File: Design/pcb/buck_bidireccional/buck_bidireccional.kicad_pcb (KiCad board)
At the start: 2 copper layers, 85 x 60 mm, 19 parts, among them J1 Conn_01x02_Pin, J2 Screw_Terminal_01x02, J3 Screw_Terminal_01x02, J4 Conn_01x02_Pin, Q1 NMOS, Q2 NMOS, U1 IR2184

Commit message: updated pcb
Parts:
- added C4: 4.7u, Capacitor_THT:CP_Radial_D5.0mm_P2.00mm, F.Cu at (154.5, 120.5)
- added J5: Screw_Terminal_01x02, TerminalBlock_Phoenix:TerminalBlock_Phoenix_MKDS-1,5-2-5.08_1x02_P5.08mm_Horizontal, F.Cu at (117.5, 126.1)
- added R6: 10k, Resistor_THT:R_Axial_DIN0207_L6.3mm_D2.5mm_P7.62mm_Horizontal, F.Cu at (128.2, 129.8)
- R4, R5: value 100k -> 10k
- moved Q2 35.6 mm to (139.7, 93.5), turned to 0 degrees
- moved R5 28.3 mm to (148.2, 98.4), turned to -90 degrees
- moved R3 18.3 mm to (122.2, 104.8)
- moved J1 18.0 mm to (133.2, 129.2), turned to 90 degrees
- moved D2 16.8 mm to (127.8, 104.8)
- moved R4 15.0 mm to (133.2, 96.9), turned to -90 degrees
- moved R1 14.1 mm to (149.5, 121.9), turned to -90 degrees
- moved R2 13.4 mm to (139.0, 105.6), turned to 90 degrees
- moved D3 12.8 mm to (143.5, 106.1), turned to 90 degrees
- moved Q1 12.3 mm to (127.7, 93.5)
- moved D4 11.7 mm to (137.7, 122.0)
- moved U1 10.6 mm to (133.2, 116.3), turned to 90 degrees
- moved C3 8.88 mm to (147.5, 112.8), turned to 0 degrees
- moved C1 7.58 mm to (125.8, 111.8)
- moved J3 6.37 mm to (115.9, 110.7)
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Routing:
- net GND: track 143.8 -> 0.00 mm
- net Net-(D2-K): track 12.8 -> 120.6 mm
- net Net-(D4-K): track 9.27 -> 109.4 mm
- net +12V: track 28.0 -> 88.6 mm
- net Net-(J4-Pin_2): track 132.8 -> 101.9 mm
- net Net-(D2-A): track 11.9 -> 27.4 mm
- net Net-(J1-Pin_2): track 33.8 -> 27.6 mm
- net Net-(J1-Pin_1): track 24.3 -> 18.6 mm
- net Net-(D3-K): track 10.8 -> 16.1 mm
- net Net-(J2-Pin_1): track 51.7 -> 56.4 mm
- net Net-(D3-A): track 11.1 -> 14.9 mm
- net Net-(J3-Pin_1): track 30.0 -> 29.2 mm
- added copper zone on F.Cu, net (none)
- added copper zone on F.Cu, net GND

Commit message: updates kiskas
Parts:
- moved J2 5.12 mm to (171.0, 127.2), turned to 0 degrees
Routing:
- net Net-(J2-Pin_1): track 56.4 -> 55.6 mm

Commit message: update kicad
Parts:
- C4: value 4.7u -> 100n
- moved J2 55.0 mm to (116.0, 127.2), turned to -90 degrees
- moved J5 51.1 mm to (168.5, 128.5)
- moved C2 48.4 mm to (125.2, 128.5), turned to -90 degrees
- moved J4 48.3 mm to (135.0, 131.8), turned to 90 degrees
- moved R3 48.2 mm to (168.3, 90.5), turned to 180 degrees
- moved J1 43.7 mm to (173.0, 111.0), turned to 180 degrees
- moved D2 41.9 mm to (168.3, 94.2), turned to 180 degrees
- moved R6 41.6 mm to (167.1, 114.8), turned to 180 degrees
- moved R2 38.5 mm to (176.8, 97.8)
- moved U1 36.5 mm to (167.1, 102.7), turned to -90 degrees
- moved R1 29.3 mm to (177.0, 111.9)
- moved R5 28.9 mm to (177.0, 101.7)
- moved D3 28.5 mm to (171.8, 102.1)
- moved L1 24.2 mm to (142.5, 108.8), turned to 90 degrees
- moved R4 20.8 mm to (154.0, 97.3), turned to 90 degrees
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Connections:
- C4 pad 1: Net-(D2-K) -> +12V
- C4 pad 2: Net-(J4-Pin_2) -> GND
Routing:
- net Net-(D2-K): track 120.6 -> 38.9 mm
- net Net-(D4-K): track 109.4 -> 32.9 mm
- net +12V: track 88.6 -> 27.8 mm
- net Net-(J2-Pin_1): track 55.6 -> 0.46 mm
- net Net-(D3-A): track 14.9 -> 65.1 mm
- net Net-(J3-Pin_1): track 29.2 -> 0.00 mm
- net Net-(D2-A): track 27.4 -> 40.5 mm
- net Net-(J4-Pin_2): track 101.9 -> 109.3 mm
- net Net-(D3-K): track 16.1 -> 21.1 mm
- net Net-(J1-Pin_2): track 27.6 -> 32.1 mm
- added copper zone on B.Cu, net +12V
- added copper zone on B.Cu, net GND
- added copper zone on B.Cu, net Net-(J2-Pin_1)
- added copper zone on B.Cu, net Net-(J3-Pin_1)
- added copper zone on B.Cu, net Net-(J4-Pin_2)
- removed copper zone on F.Cu, net (none)
- removed copper zone on F.Cu, net GND

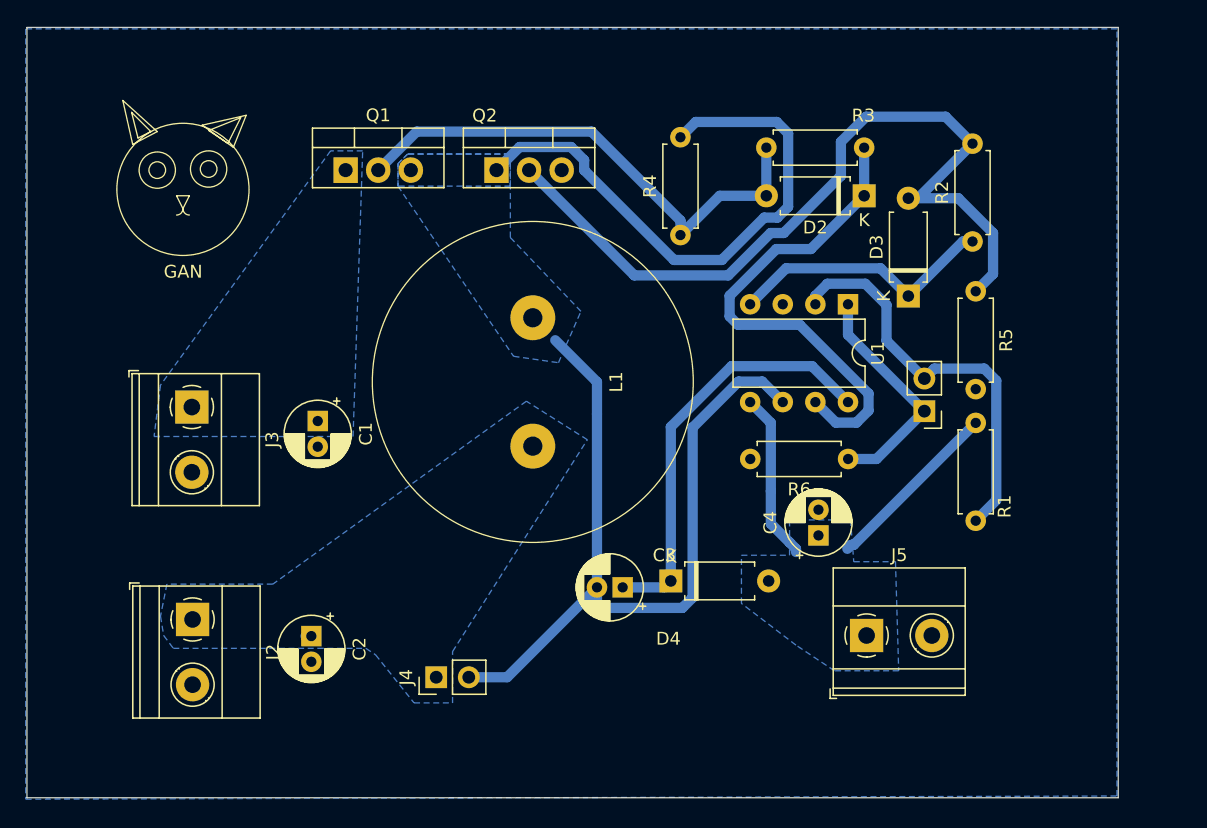
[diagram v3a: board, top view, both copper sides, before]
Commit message: updated kicad
MOSFET gate oscilloscope reading still missing
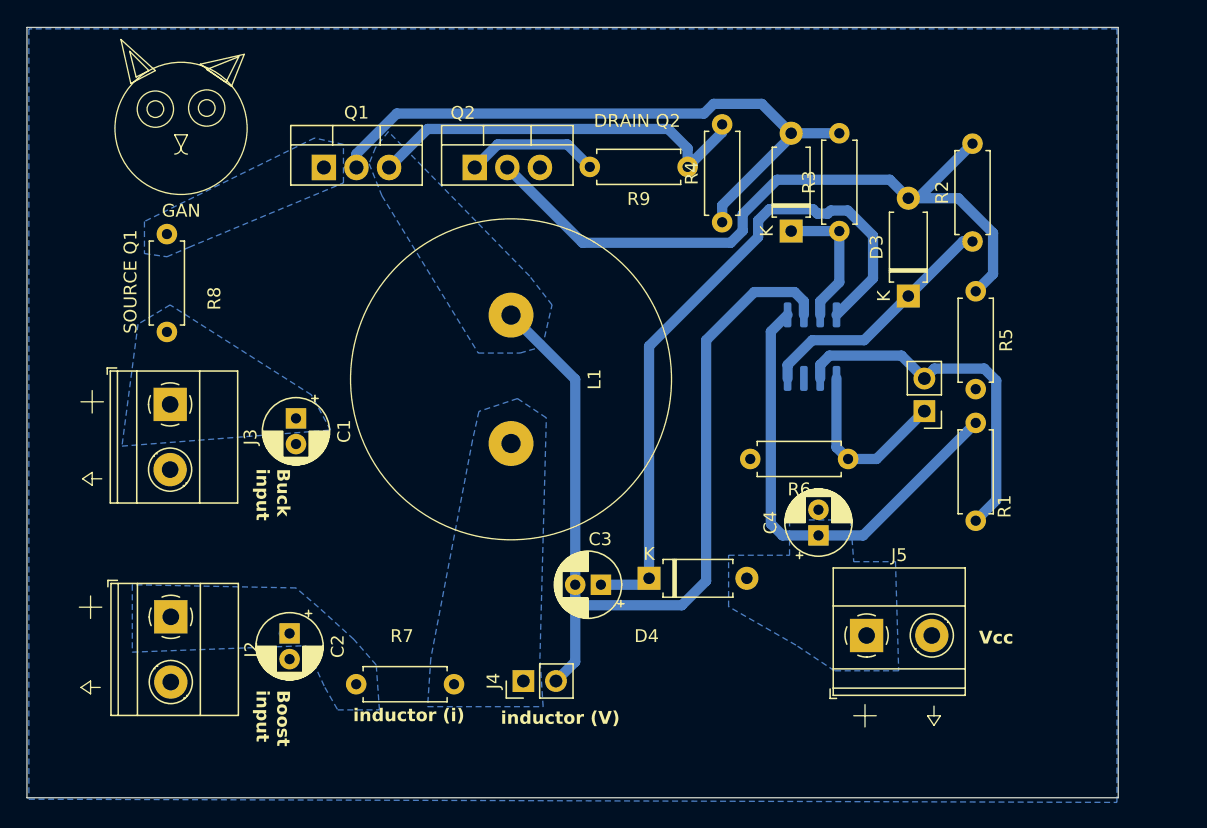
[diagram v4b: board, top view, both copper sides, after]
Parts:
- added R7: 1, Resistor_THT:R_Axial_DIN0207_L6.3mm_D2.5mm_P7.62mm_Horizontal, F.Cu at (136.4, 132.3)
- added R8: 1, Resistor_THT:R_Axial_DIN0207_L6.3mm_D2.5mm_P7.62mm_Horizontal, F.Cu at (114.0, 104.9)
- added R9: 1, Resistor_THT:R_Axial_DIN0207_L6.3mm_D2.5mm_P7.62mm_Horizontal, F.Cu at (146.9, 92.0)
- U1: footprint Package_DIP:DIP-8_W7.62mm -> Package_SO:SOIC-8_3.9x4.9mm_P1.27mm; moved to B.Cu
- moved J4 6.80 mm to (141.8, 132.0)
- moved R3 6.78 mm to (166.4, 97.0), turned to 90 degrees
- moved D2 6.32 mm to (162.6, 97.0), turned to 90 degrees
- moved U1 4.33 mm to (164.2, 106.0), turned to 90 degrees
- moved R4 3.40 mm to (157.2, 96.3)
- moved Q1 1.71 mm to (126.2, 92.0)
- moved C1 1.71 mm to (124.1, 111.6)
- moved C3 1.71 mm to (147.8, 124.5)
- moved D4 1.71 mm to (151.6, 124.0)
- moved J2 1.71 mm to (114.3, 127.0)
- moved J3 1.71 mm to (114.2, 110.5)
- moved L1 1.71 mm to (140.8, 108.5)
- moved Q2 1.71 mm to (138.0, 92.0)
- moved C2 1.71 mm to (123.6, 128.3)
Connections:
- J4 pad 1: Net-(J2-Pin_1) -> Net-(J4-Pin_1)
- L1 pad 1: Net-(J2-Pin_1) -> Net-(J4-Pin_1)
- Q1 pad 1: Net-(J3-Pin_1) -> Net-(Q1-D)
- Q2 pad 1: Net-(J4-Pin_2) -> Net-(Q2-D)
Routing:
- net Net-(D2-K): track 38.9 -> 10.9 mm
- net Net-(D4-K): track 32.9 -> 53.1 mm
- net Net-(Q2-D): track 0.00 -> 10.4 mm
- net Net-(D2-A): track 40.5 -> 50.4 mm
- net +12V: track 27.8 -> 36.8 mm
- net Net-(D3-A): track 65.1 -> 56.6 mm
- net Net-(J4-Pin_2): track 109.3 -> 102.8 mm
- net Net-(J1-Pin_1): track 18.3 -> 14.1 mm
- net Net-(J1-Pin_2): track 32.1 -> 28.1 mm
- net Net-(D3-K): track 21.1 -> 19.5 mm
- added copper zone on B.Cu, net Net-(J4-Pin_1)
- added copper zone on B.Cu, net Net-(Q1-D)
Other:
- board text added: "Boost input"
- board text added: "Buck input"
- board text added: "DRAIN Q2"
- board text added: "SOURCE Q1"
- board text added: "Vcc"
- board text added: "inductor (V)"
- board text added: "inductor (i)"

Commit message: final kicad
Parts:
- removed R7, R8, R9: 1, Resistor_THT:R_Axial_DIN0207_L6.3mm_D2.5mm_P7.62mm_Horizontal
- added DQ1: TestPoint, TestPoint:TestPoint_Bridge_Pitch2.54mm_Drill0.7mm, F.Cu at (113.0, 99.5)
- added DQ2: TestPoint, TestPoint:TestPoint_Bridge_Pitch2.54mm_Drill0.7mm, F.Cu at (141.8, 133.5)
- added IL1: TestPoint, TestPoint:TestPoint_Bridge_Pitch2.54mm_Drill0.7mm, F.Cu at (125.7, 134.0)
- added Vgs_Q1: Conn_01x02_Pin, Connector_PinHeader_2.54mm:PinHeader_1x02_P2.54mm_Vertical, F.Cu at (131.8, 95.5)
- added Vgs_Q2: Conn_01x02_Pin, Connector_PinHeader_2.54mm:PinHeader_1x02_P2.54mm_Vertical, F.Cu at (179.0, 95.8)
- moved D3 25.3 mm to (146.5, 103.1)
- moved R5 15.1 mm to (162.5, 97.4)
- moved U1 14.9 mm to (150.0, 110.5), turned to 180 degrees
- moved R6 13.0 mm to (155.7, 108.5), turned to 0 degrees
- moved R1 11.6 mm to (169.0, 120.3), turned to 90 degrees
- moved D2 9.99 mm to (154.5, 102.8)
- moved Vl1 9.16 mm to (132.7, 133.5)
- moved L1 9.04 mm to (134.0, 114.5), turned to 0 degrees
- moved R2 8.93 mm to (175.3, 89.0), turned to 180 degrees
- moved R3 8.31 mm to (164.1, 89.0), turned to 180 degrees
- moved R4 7.92 mm to (150.0, 93.1), turned to -90 degrees
- moved PWM1 6.73 mm to (176.5, 116.8)
- moved D4 4.96 mm to (149.4, 128.5)
- moved Q2 4.37 mm to (142.0, 90.2)
- moved C3 4.11 mm to (144.0, 123.0)
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- renumbered J1 to PWM1, J5 to Vcc1, J4 to Vl1
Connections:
- net Net-(D2-A) renamed HO
- net Net-(D3-A) renamed LO
- C3 pad 2: Net-(J4-Pin_2) -> VS
- L1 pad 1: Net-(J4-Pin_1) -> Net-(J2-Pin_1)
- L1 pad 2: Net-(J4-Pin_2) -> VS
- Q1 pad 1: Net-(Q1-D) -> Net-(J3-Pin_1)
- Q1 pad 3: Net-(J4-Pin_2) -> VS
- Q2 pad 1: Net-(Q2-D) -> VS
- R4 pad 2: Net-(J4-Pin_2) -> VS
- U1 pad 6: Net-(J4-Pin_2) -> VS
- Vl1 pad 1: Net-(J4-Pin_1) -> Net-(J2-Pin_1)
- Vl1 pad 2: Net-(J4-Pin_2) -> VS
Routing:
- net Net-(J4-Pin_2): track 102.8 -> 0.00 mm
- net VS: track 0.00 -> 59.6 mm
- net Net-(D2-K): track 10.9 -> 46.4 mm
- net Net-(D4-K): track 53.1 -> 24.2 mm
- net Net-(D3-K): track 19.5 -> 46.5 mm
- net +12V: track 36.8 -> 17.8 mm
- net Net-(PWM1-Pin_1): track 14.1 -> 31.7 mm
- net Net-(Q2-D): track 10.4 -> 0.00 mm
- net LO: track 56.6 -> 54.1 mm
- net Net-(PWM1-Pin_2): track 28.1 -> 25.8 mm
- added copper zone on B.Cu, net VS
- removed copper zone on B.Cu, net Net-(J4-Pin_1)
- removed copper zone on B.Cu, net Net-(J4-Pin_2)
- removed copper zone on B.Cu, net Net-(Q1-D)
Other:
- board text added: "G1"
- board text added: "IL"
- board text added: "PWM"
- board text added: "VL"
- board text added: "Vgs Q1"
- board text added: "Vgs Q2"
- board text removed: "inductor (V)"
- board text removed: "inductor (i)"

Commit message: g1 to g2
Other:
- board text added: "G2"
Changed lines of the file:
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@@
 		)
 	)
-	(gr_text "G1\n"
+	(gr_text "G2"
 		(at 169.75 91 180)
 		(layer "F.SilkS")

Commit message: final pcb
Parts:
- L1: footprint BUCK_INDUCTOR:buck_inductor -> inductores:buck_inductor
- moved C1 1.34 mm to (124.0, 110.2)
- moved R1 1.06 mm to (169.0, 121.4)
- moved R4 1.00 mm to (151.0, 93.1)
- moved J3 0.75 mm to (114.2, 109.8)
- moved Q2 0.54 mm to (141.7, 90.7)
- moved Q1 0.31 mm to (126.2, 90.8)
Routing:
- net Net-(J2-Pin_1): track 0.00 -> 7.20 mm
- net HO: track 50.5 -> 48.5 mm
- net LO: track 54.1 -> 55.2 mm
- net VS: track 59.6 -> 60.6 mm
- net Net-(D3-K): track 46.5 -> 45.7 mm
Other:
- board text added: "DQ2"
- board text added: "K"
- board text added: "SQ1"
- board text removed: "DRAIN Q2"
- board text removed: "GAN"
- board text removed: "SOURCE Q1"

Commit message: update kicad + gerber
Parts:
- moved PWM1 5.59 mm to (177.0, 111.2), turned to 0 degrees
- moved D3 2.30 mm to (147.0, 105.3)
- moved R3 1.60 mm to (163.6, 90.5)
- moved R2 1.58 mm to (174.8, 90.5)
- moved D2 0.75 mm to (154.5, 102.1)
- moved Vgs_Q1 0.49 mm to (131.3, 95.5)
- turned R5 to 0 degrees
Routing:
- net LO: track 55.2 -> 63.7 mm
- net Net-(J2-Pin_1): track 7.20 -> 0.00 mm
- net HO: track 48.5 -> 42.0 mm
- net Net-(PWM1-Pin_1): track 31.7 -> 25.7 mm
- net Net-(D2-K): track 46.4 -> 44.2 mm
- net VS: track 60.6 -> 58.5 mm
- net Net-(D3-K): track 45.7 -> 46.9 mm
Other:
- board text added: "1"
